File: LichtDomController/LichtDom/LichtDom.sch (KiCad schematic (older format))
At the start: 38 parts, among them J101 Conn_01x02_Male, J102 Raspberry_Pi_2_3, J103 Stecker der Lichtdomplatten, J104 Stecker des Zweifarb-Ringlich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, J105 0,96\" OLED, U1 TPS5430DDA, U101 74HC595, U102 74HC595, U103 74HC595

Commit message: beginn vom pcb hinzugefügt...
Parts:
- added MK101, MK102, MK103, MK104: Mounting_Hole, MountingHole:MountingHole_3.2mm_M3, symbol Mechanical:Mounting_Hole
- added MK105, MK106, MK107, MK108: Mounting_Hole, MountingHole:MountingHole_3.2mm_M3_DIN965, symbol Mechanical:Mounting_Hole
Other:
- note added: "OLED-Montagelöcher"
- note added: "Platinenanschlusslöcher"
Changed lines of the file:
@@
 Wire Wire Line
 	5750 4300 5450 4300
+$Comp
+L Mechanical:Mounting_Hole MK105
+U 1 1 5DF0CFCD
+P 5750 3000
+F 0 "MK105" H 5850 3046 50  0000 L CNN
+F 1 "Mounting_Hole" H 5850 2955 50  0000 L CNN
+F 2 "MountingHole:MountingHole_3.2mm_M3_DIN965" H 5750 3000 50  0001 C CNN
+F 3 "" H 5750 3000 50  0001 C CNN
+	1    5750 3000
+	1    0    0    -1
+$EndComp
+$Comp
+L Mechanical:Mounting_Hole MK106
+U 1 1 5DF0D94C
+P 5750 3250
+F 0 "MK106" H 5850 3296 50  0000 L CNN
+F 1 "Mounting_Hole" H 5850 3205 50  0000 L CNN
+F 2 "MountingHole:MountingHole_3.2mm_M3_DIN965" H 5750 3250 50  0001 C CNN
+F 3 "" H 5750 3250 50  0001 C CNN
+	1    5750 3250
+	1    0    0    -1
+$EndComp
+$Comp
+L Mechanical:Mounting_Hole MK107
+U 1 1 5DF0DC9F
+P 5750 3500
+F 0 "MK107" H 5850 3546 50  0000 L CNN
+F 1 "Mounting_Hole" H 5850 3455 50  0000 L CNN
+F 2 "MountingHole:MountingHole_3.2mm_M3_DIN965" H 5750 3500 50  0001 C CNN
+F 3 "" H 5750 3500 50  0001 C CNN
+	1    5750 3500
+	1    0    0    -1
+$EndComp
+$Comp
+L Mechanical:Mounting_Hole MK108
+U 1 1 5DF0DF98
+P 5750 3750
+F 0 "MK108" H 5850 3796 50  0000 L CNN
+F 1 "Mounting_Hole" H 5850 3705 50  0000 L CNN
+F 2 "MountingHole:MountingHole_3.2mm_M3_DIN965" H 5750 3750 50  0001 C CNN
+F 3 "" H 5750 3750 50  0001 C CNN
+	1    5750 3750
+	1    0    0    -1
+$EndComp
+$Comp
+L Mechanical:Mounting_Hole MK103
+U 1 1 5DF10368
+P 5500 6500
+F 0 "MK103" H 5600 6546 50  0000 L CNN
+F 1 "Mounting_Hole" H 5600 6455 50  0000 L CNN
+F 2 "MountingHole:MountingHole_3.2mm_M3" H 5500 6500 50  0001 C CNN
+F 3 "" H 5500 6500 50  0001 C CNN
+	1    5500 6500
+	1    0    0    -1
+$EndComp
+$Comp
+L Mechanical:Mounting_Hole MK101
+U 1 1 5DF10374
+P 5500 6000
+F 0 "MK101" H 5600 6046 50  0000 L CNN
+F 1 "Mounting_Hole" H 5600 5955 50  0000 L CNN
+F 2 "MountingHole:MountingHole_3.2mm_M3" H 5500 6000 50  0001 C CNN
+F 3 "" H 5500 6000 50  0001 C CNN
+	1    5500 6000
+	1    0    0    -1
+$EndComp
+$Comp
+L Mechanical:Mounting_Hole MK102
+U 1 1 5DF10380
+P 5500 6250
+F 0 "MK102" H 5600 6296 50  0000 L CNN
+F 1 "Mounting_Hole" H 5600 6205 50  0000 L CNN
+F 2 "MountingHole:MountingHole_3.2mm_M3" H 5500 6250 50  0001 C CNN
+F 3 "" H 5500 6250 50  0001 C CNN
+	1    5500 6250
+	1    0    0    -1
+$EndComp
+$Comp
+L Mechanical:Mounting_Hole MK104
+U 1 1 5DF1038C
+P 5500 6750
+F 0 "MK104" H 5600 6796 50  0000 L CNN
+F 1 "Mounting_Hole" H 5600 6705 50  0000 L CNN
+F 2 "MountingHole:MountingHole_3.2mm_M3" H 5500 6750 50  0001 C CNN
+F 3 "" H 5500 6750 50  0001 C CNN
+	1    5500 6750
+	1    0    0    -1
+$EndComp
+Text Notes 5500 5800 0    50   ~ 0
+Platinenanschlusslöcher
+Text Notes 5750 2800 0    50   ~ 0
+OLED-Montagelöcher
 $EndSCHEMATC

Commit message: Layout quasi fertig - Texte ausgerichtet. Teilweise fehlen noch 3D-Daten!
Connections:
- net +5V: now also C5.1, C6.1, C7.1, L1.1, R3.1, TP104.1
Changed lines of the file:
@@
 Text Notes 5750 2800 0    50   ~ 0
 OLED-Montagelöcher
+$Comp
+L power:+5V #PWR?
+U 1 1 5DE6E388
+P 6700 1200
+F 0 "#PWR?" H 6700 1050 50  0001 C CNN
+F 1 "+5V" H 6715 1373 50  0000 C CNN
+F 2 "" H 6700 1200 50  0001 C CNN
+F 3 "" H 6700 1200 50  0001 C CNN
+	1    6700 1200
+	1    0    0    -1
+$EndComp
 $EndSCHEMATC

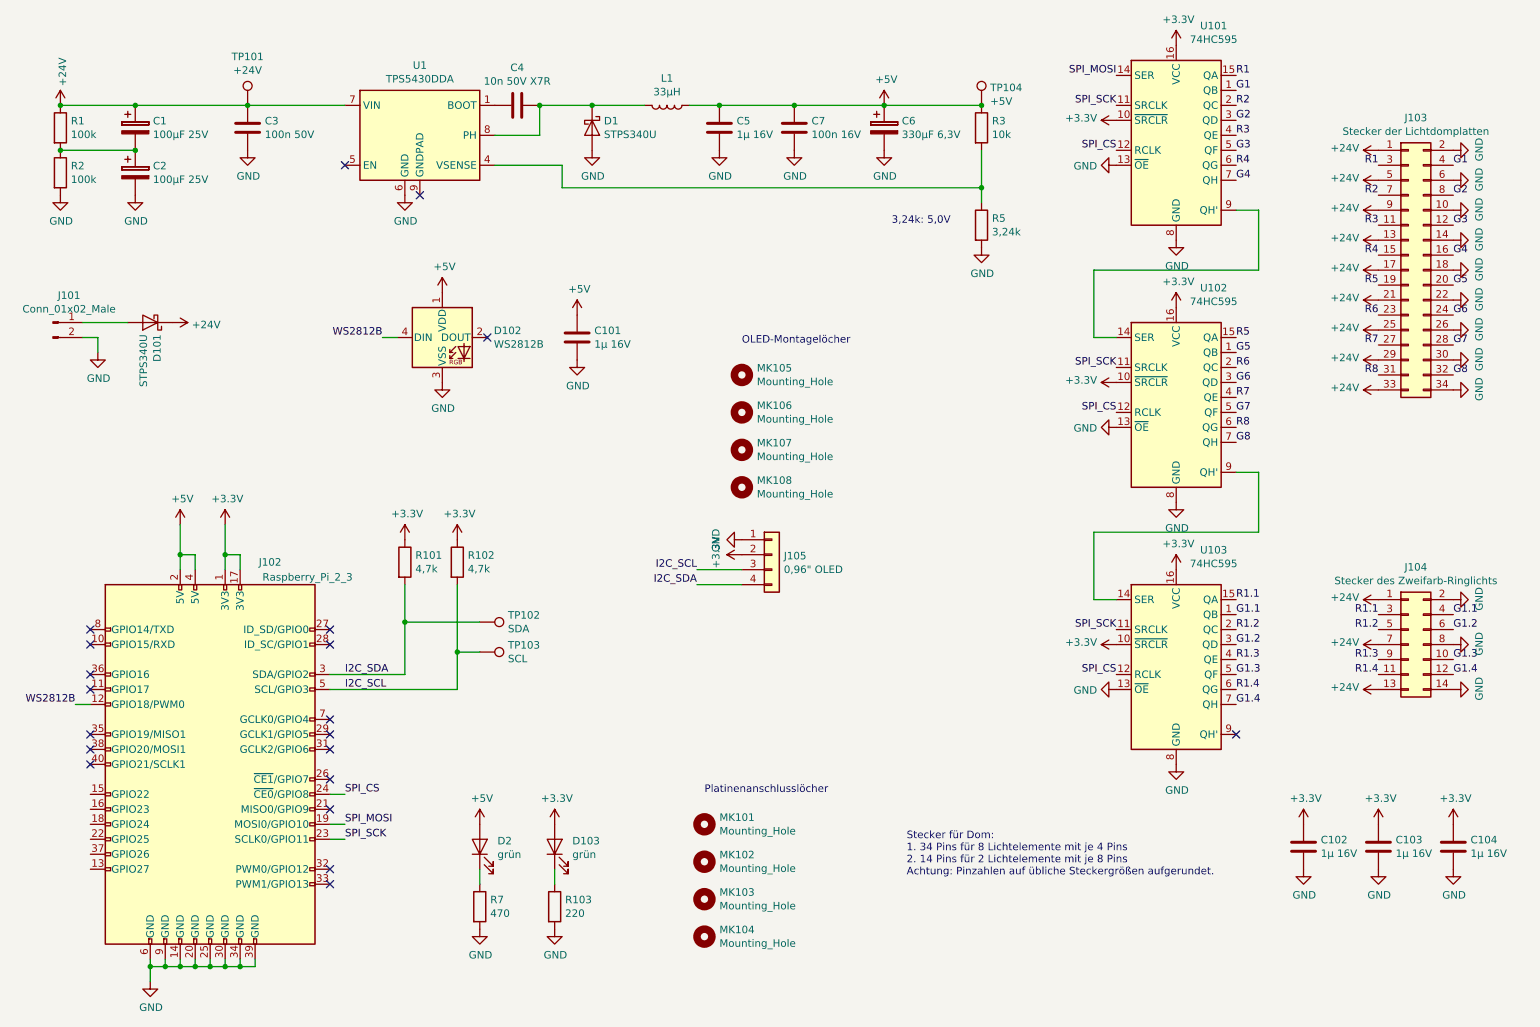
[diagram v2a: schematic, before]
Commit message: Lüfteranschluss hinzufügt.
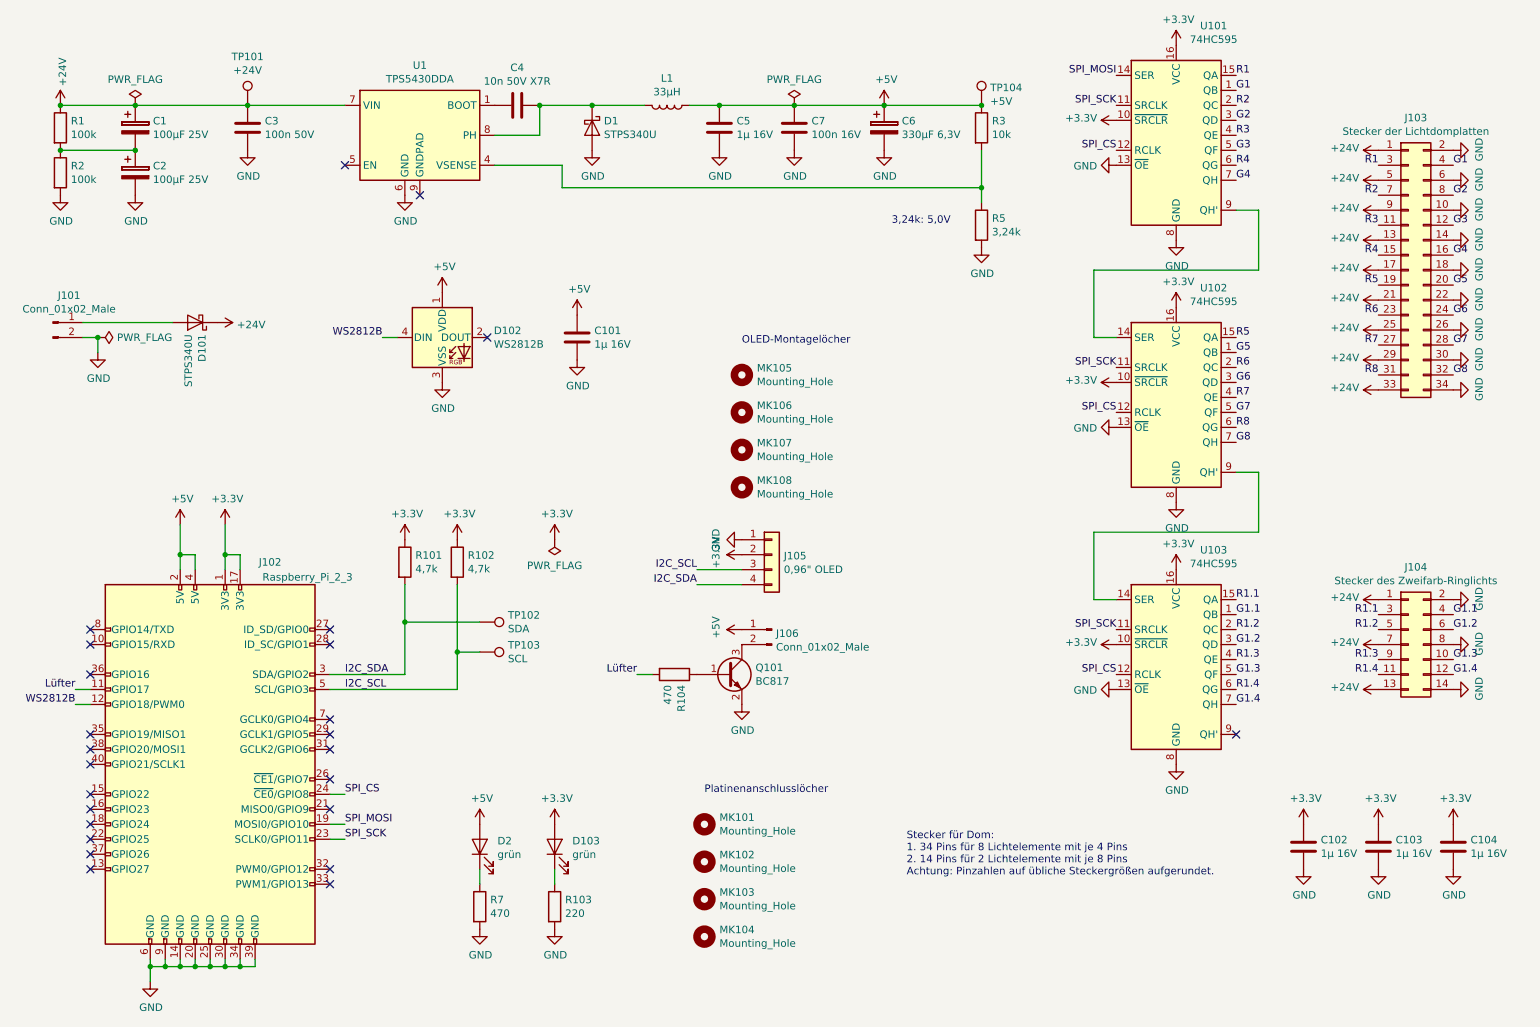
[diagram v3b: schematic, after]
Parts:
- added J106: Conn_01x02_Male, Connector_JST:JST_PH_S2B-PH-SM4-TB_1x02-1MP_P2.00mm_Horizontal, symbol Connector:Conn_01x02_Male
- added Q101: BC817, Package_TO_SOT_SMD:SOT-23, symbol Transistor_BJT:BC817
- added R104: 470, Resistor_SMD:R_0603_1608Metric, symbol Device:R
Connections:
- net +5V: now also J106.1 (Pin_1)
- net GND: now also Q101.2 (E)
- net Lüfter: now reaches J102.11 (GPIO17)
- net Lüfter: now also R104.2
- new net: J106.2 (Pin_2), Q101.3 (C)
- new net: Q101.1 (B), R104.1
- no-connect marks 20 -> 25
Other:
- moved on the sheet: D101
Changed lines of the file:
@@
 L power:+24V #PWR0109
 U 1 1 5DE3C300
-P 1950 2650
-F 0 "#PWR0109" H 1950 2500 50  0001 C CNN
-F 1 "+24V" V 1965 2778 50  0000 L CNN
-F 2 "" H 1950 2650 50  0001 C CNN
-F 3 "" H 1950 2650 50  0001 C CNN
-	1    1950 2650
+P 2250 2650
+F 0 "#PWR0109" H 2250 2500 50  0001 C CNN
+F 1 "+24V" V 2265 2778 50  0000 L CNN
+F 2 "" H 2250 2650 50  0001 C CNN
+F 3 "" H 2250 2650 50  0001 C CNN
+	1    2250 2650
 	0    1    1    0
 $EndComp
-Wire Wire Line
-	1650 2650 1350 2650
 $Comp
 L power:GND #PWR0103
@@
 L Device:D_Schottky D101
 U 1 1 5DEB3539
-P 1800 2650
-F 0 "D101" V 1754 2729 50  0000 L CNN
-F 1 "STPS340U" V 1845 2729 50  0000 L CNN
-F 2 "Diode_SMD:D_SMB" H 1800 2650 50  0001 C CNN
-F 3 "https://www.st.com/resource/en/datasheet/CD00000844.pdf" H 1800 2650 50  0001 C CNN
-	1    1800 2650
+P 2100 2650
+F 0 "D101" V 2054 2729 50  0000 L CNN
+F 1 "STPS340U" V 2145 2729 50  0000 L CNN
+F 2 "Diode_SMD:D_SMB" H 2100 2650 50  0001 C CNN
+F 3 "https://www.st.com/resource/en/datasheet/CD00000844.pdf" H 2100 2650 50  0001 C CNN
+	1    2100 2650
 	-1   0    0    1
 $EndComp
@@
 NoConn ~ 3000 5500
 NoConn ~ 1400 5000
-NoConn ~ 1400 5100
 Text Label 1300 5200 2    50   ~ 0
 WS2812B
@@
 OLED-Montagelöcher
 $Comp
-L power:+5V #PWR?
+L power:+5V #PWR0168
 U 1 1 5DE6E388
 P 6700 1200
-F 0 "#PWR?" H 6700 1050 50  0001 C CNN
+F 0 "#PWR0168" H 6700 1050 50  0001 C CNN
 F 1 "+5V" H 6715 1373 50  0000 C CNN
 F 2 "" H 6700 1200 50  0001 C CNN
@@
 	1    0    0    -1
 $EndComp
+$Comp
+L Connector:Conn_01x02_Male J106
+U 1 1 5DE98246
+P 5950 4700
+F 0 "J106" H 5922 4674 50  0000 R CNN
+F 1 "Conn_01x02_Male" H 5922 4583 50  0000 R CNN
+F 2 "Connector_JST:JST_PH_S2B-PH-SM4-TB_1x02-1MP_P2.00mm_Horizontal" H 5950 4700 50  0001 C CNN
+F 3 "~" H 5950 4700 50  0001 C CNN
+	1    5950 4700
+	-1   0    0    -1
+$EndComp
+$Comp
+L power:+5V #PWR0169
+U 1 1 5DE98C68
+P 5750 4700
+F 0 "#PWR0169" H 5750 4550 50  0001 C CNN
+F 1 "+5V" H 5765 4873 50  0000 C CNN
+F 2 "" H 5750 4700 50  0001 C CNN
+F 3 "" H 5750 4700 50  0001 C CNN
+	1    5750 4700
+	0    -1   -1   0
+$EndComp
+$Comp
+L Transistor_BJT:BC817 Q101
+U 1 1 5DE99889
+P 5650 5000
+F 0 "Q101" H 5841 5046 50  0000 L CNN
+F 1 "BC817" H 5841 4955 50  0000 L CNN
+F 2 "Package_TO_SOT_SMD:SOT-23" H 5850 4925 50  0001 L CIN
+F 3 "http://www.fairchildsemi.com/ds/BC/BC817.pdf" H 5650 5000 50  0001 L CNN
+	1    5650 5000
+	1    0    0    -1
+$EndComp
+$Comp
+L power:GND #PWR0170
+U 1 1 5DE9AC84
+P 5750 5200
+F 0 "#PWR0170" H 5750 4950 50  0001 C CNN
+F 1 "GND" H 5755 5027 50  0000 C CNN
+F 2 "" H 5750 5200 50  0001 C CNN
+F 3 "" H 5750 5200 50  0001 C CNN
+	1    5750 5200
+	1    0    0    -1
+$EndComp
+$Comp
+L Device:R R104
+U 1 1 5DE9B0C0
+P 5300 5000
+F 0 "R104" H 5370 5046 50  0000 L CNN
+F 1 "470" H 5370 4955 50  0000 L CNN
+F 2 "Resistor_SMD:R_0603_1608Metric" V 5230 5000 50  0001 C CNN
+F 3 "~" H 5300 5000 50  0001 C CNN
+	1    5300 5000
+	0    1    1    0
+$EndComp
+Text Label 1300 5100 2    50   ~ 0
+Lüfter
+Wire Wire Line
+	1400 5100 1300 5100
+Text Label 5050 5000 2    50   ~ 0
+Lüfter
+Wire Wire Line
+	5050 5000 5150 5000
+NoConn ~ 1400 6300
+NoConn ~ 1400 6200
+NoConn ~ 1400 6100
+NoConn ~ 1400 6000
+NoConn ~ 1400 5900
+NoConn ~ 1400 5800
+$Comp
+L power:PWR_FLAG #FLG0101
+U 1 1 5DE9E35C
+P 6100 1200
+F 0 "#FLG0101" H 6100 1275 50  0001 C CNN
+F 1 "PWR_FLAG" H 6100 1373 50  0000 C CNN
+F 2 "" H 6100 1200 50  0001 C CNN
+F 3 "~" H 6100 1200 50  0001 C CNN
+	1    6100 1200
+	1    0    0    -1
+$EndComp
+$Comp
+L power:PWR_FLAG #FLG0102
+U 1 1 5DE9EB51
+P 1700 1200
+F 0 "#FLG0102" H 1700 1275 50  0001 C CNN
+F 1 "PWR_FLAG" H 1700 1373 50  0000 C CNN
+F 2 "" H 1700 1200 50  0001 C CNN
+F 3 "~" H 1700 1200 50  0001 C CNN
+	1    1700 1200
+	1    0    0    -1
+$EndComp
+$Comp
+L power:PWR_FLAG #FLG0103
+U 1 1 5DEA02BB
+P 1450 2750
+F 0 "#FLG0103" H 1450 2825 50  0001 C CNN
+F 1 "PWR_FLAG" V 1450 2878 50  0000 L CNN
+F 2 "" H 1450 2750 50  0001 C CNN
+F 3 "~" H 1450 2750 50  0001 C CNN
+	1    1450 2750
+	0    1    1    0
+$EndComp
+Connection ~ 1450 2750
+Wire Wire Line
+	1350 2650 1950 2650
+$Comp
+L power:+3.3V #PWR0171
+U 1 1 5DEA1818
+P 4500 4100
+F 0 "#PWR0171" H 4500 3950 50  0001 C CNN
+F 1 "+3.3V" H 4515 4273 50  0000 C CNN
+F 2 "" H 4500 4100 50  0001 C CNN
+F 3 "" H 4500 4100 50  0001 C CNN
+	1    4500 4100
+	1    0    0    -1
+$EndComp
+$Comp
+L power:PWR_FLAG #FLG0104
+U 1 1 5DEA21DB
+P 4500 4100
+F 0 "#FLG0104" H 4500 4175 50  0001 C CNN
+F 1 "PWR_FLAG" H 4500 4273 50  0000 C CNN
+F 2 "" H 4500 4100 50  0001 C CNN
+F 3 "~" H 4500 4100 50  0001 C CNN
+	1    4500 4100
+	-1   0    0    1
+$EndComp
 $EndSCHEMATC
